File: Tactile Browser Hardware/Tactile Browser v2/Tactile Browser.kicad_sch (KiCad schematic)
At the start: 79 parts, among them SW1 SW_Push, SW10 SW_Push, SW11 SW_Push, SW12 SW_Push, SW13 SW_Push, SW14 SW_Push, SW15 SW_Push, SW16 SW_Push, SW17 SW_Push, SW18 SW_Push, SW19 SW_Push, SW2 SW_Push, SW20 SW_Push, SW3 SW_Push, SW4 SW_Push, SW5 SW_Push, SW6 SW_Push, SW7 SW_Push, SW8 SW_Push, SW9 SW_Push

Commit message: updated module schematic
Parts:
- removed D16, D17: 1N4148, Diode_THT:D_DO-35_SOD27_P7.62mm_Horizontal, symbol Diode:1N4148
- removed Driver10: TB6612FNG, TB6612FNG_THT:TB6612FNG_DualPinHeader_1x8x2_P2.54mm_Row15.24mm_THT, symbol Driver_Motor:TB6612FNG
- removed SW19, SW20: SW_Push, TerminalBlock:TerminalBlock_Xinya_XY308-2.54-2P_1x02_P2.54mm_Horizontal, symbol Switch:SW_Push
- removed Solenoid19, Solenoid20: Conn_01x02_Pin, Connector_JST:JST_VH_B2P-VH-B_1x02_P3.96mm_Vertical, symbol Connector:Conn_01x02_Pin
- added SPI1: Conn_01x03_Pin, TerminalBlock:TerminalBlock_Xinya_XY308-2.54-3P_1x03_P2.54mm_Horizontal, symbol Connector:Conn_01x03_Pin
- renumbered SW9 to SW10, SW10 to SW11, SW17 to SW12, SW11 to SW13, SW12 to SW14, SW13 to SW15, SW14 to SW16, SW15 to SW17, SW16 to SW6, SW6 to SW7, SW7 to SW8, SW8 to SW9
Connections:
- net CLOCK: now also SPI1.1 (Pin_1); no longer A1.16 (D13)
- net Col1: now also A1.2 (D0/RX), D1.1 (K), D19.1 (K), D2.1 (K), D3.1 (K), D4.1 (K), D5.1 (K); no longer A1.7 (D4), SW1.2, SW13.2, SW6.2, SW7.2
- net Col2: now also A1.1 (D1/TX), D14.1 (K), D20.1 (K), D6.1 (K), D7.1 (K), D8.1 (K), D9.1 (K); no longer A1.8 (D5), SW12.2, SW14.2, SW2.2, SW8.2
- net Col3: now also A1.5 (D2), D10.1 (K), D11.1 (K), D12.1 (K), D13.1 (K), D15.1 (K), D18.1 (K); no longer A1.9 (D6), SW15.2, SW18.2, SW3.2, SW9.2
- net DATA: now also SPI1.2 (Pin_2); no longer A1.14 (D11)
- net LATCH: now also SPI1.3 (Pin_3); no longer A1.13 (D10)
- net Row1: now also A1.6 (D3), SW1.2, SW13.2, SW7.2; no longer A1.2 (D0/RX), D1.1 (K), D2.1 (K), D3.1 (K), D4.1 (K), D5.1 (K)
- net Row2: now also A1.7 (D4), SW14.2, SW2.2, SW8.2; no longer A1.1 (D1/TX), D20.1 (K), D6.1 (K), D7.1 (K), D8.1 (K), D9.1 (K)
- net Row3: now also A1.8 (D5), SW15.2, SW3.2, SW9.2; no longer A1.5 (D2), D10.1 (K), D11.1 (K), D12.1 (K), D13.1 (K), D18.1 (K)
- net Row4: now also A1.9 (D6), SW10.2, SW16.2, SW4.2; no longer A1.6 (D3), D14.1 (K), D15.1 (K), D19.1 (K)
- removed net Col4: A1.10 (D7), SW10.2, SW16.2, SW4.2
- net Col5 renamed Row5
- net Row5: now also A1.10 (D7); no longer A1.11 (D8)
- net S19_in1: no longer names the net of IO_5.4 (QE)
- net S19_in2: no longer names the net of IO_5.5 (QF)
- net S20_in1: no longer names the net of IO_5.6 (QG)
- net S20_in2: no longer names the net of IO_5.7 (QH)
- new net Row6: A1.11 (D8), SW12.2, SW18.2, SW6.2
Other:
- moved on the sheet: D1, D10, D11, D12, D13, D14, D15, D18, D19, D2, D20, D3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

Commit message: updated solenoid/keyswitch connectors
for ease of manufacturing
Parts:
- removed SPI1: Conn_01x03_Pin, TerminalBlock:TerminalBlock_Xinya_XY308-2.54-3P_1x03_P2.54mm_Horizontal, symbol Connector:Conn_01x03_Pin
- D1, D2, D3, D4, D5: footprint Diode_THT:D_DO-35_SOD27_P7.62mm_Horizontal -> Diode_SMD:D_SOD-123
- D10: renamed from D9; footprint Diode_THT:D_DO-35_SOD27_P7.62mm_Horizontal -> Diode_SMD:D_SOD-123
- D11: renamed from D20; footprint Diode_THT:D_DO-35_SOD27_P7.62mm_Horizontal -> Diode_SMD:D_SOD-123
- D12: renamed from D14; footprint Diode_THT:D_DO-35_SOD27_P7.62mm_Horizontal -> Diode_SMD:D_SOD-123
- D13: renamed from D18; footprint Diode_THT:D_DO-35_SOD27_P7.62mm_Horizontal -> Diode_SMD:D_SOD-123
- D14: renamed from D10; footprint Diode_THT:D_DO-35_SOD27_P7.62mm_Horizontal -> Diode_SMD:D_SOD-123
- D15: renamed from D11; footprint Diode_THT:D_DO-35_SOD27_P7.62mm_Horizontal -> Diode_SMD:D_SOD-123
- D16: renamed from D12; footprint Diode_THT:D_DO-35_SOD27_P7.62mm_Horizontal -> Diode_SMD:D_SOD-123
- D17: renamed from D13; footprint Diode_THT:D_DO-35_SOD27_P7.62mm_Horizontal -> Diode_SMD:D_SOD-123
- D18: renamed from D15; footprint Diode_THT:D_DO-35_SOD27_P7.62mm_Horizontal -> Diode_SMD:D_SOD-123
- D6: renamed from D19; footprint Diode_THT:D_DO-35_SOD27_P7.62mm_Horizontal -> Diode_SMD:D_SOD-123
- D7: renamed from D6; footprint Diode_THT:D_DO-35_SOD27_P7.62mm_Horizontal -> Diode_SMD:D_SOD-123
- D8: renamed from D7; footprint Diode_THT:D_DO-35_SOD27_P7.62mm_Horizontal -> Diode_SMD:D_SOD-123
- D9: renamed from D8; footprint Diode_THT:D_DO-35_SOD27_P7.62mm_Horizontal -> Diode_SMD:D_SOD-123
- SW1, SW10, SW11, SW12, SW13, SW14, SW15, SW16, SW17, SW18, SW2, SW3, SW4, SW5, SW6, SW7, SW8, SW9: footprint TerminalBlock:TerminalBlock_Xinya_XY308-2.54-2P_1x02_P2.54mm_Horizontal -> Connector_JST:JST_PH_B2B-PH-SM4-TB_1x02-1MP_P2.00mm_Vertical
- Solenoid1: footprint Connector_JST:JST_VH_B2P-VH_1x02_P3.96mm_Vertical -> TerminalBlock_Phoenix:TerminalBlock_Phoenix_MKDS-1,5-2-5.08_1x02_P5.08mm_Horizontal
- Solenoid10, Solenoid11, Solenoid12, Solenoid13, Solenoid14, Solenoid15, Solenoid16, Solenoid17, Solenoid18, Solenoid2, Solenoid3, Solenoid4, Solenoid5, Solenoid6, Solenoid7, Solenoid8, Solenoid9: footprint Connector_JST:JST_VH_B2P-VH-B_1x02_P3.96mm_Vertical -> TerminalBlock_Phoenix:TerminalBlock_Phoenix_MKDS-1,5-2-5.08_1x02_P5.08mm_Horizontal
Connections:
- net 5V: now also IO_2.10 (~{SRCLR}), IO_3.10 (~{SRCLR}), IO_4.10 (~{SRCLR}), IO_5.10 (~{SRCLR})
- net CLOCK: now also A1.16 (D13)
- net DATA: now also A1.14 (D11)
- net LATCH: now also A1.13 (D10)

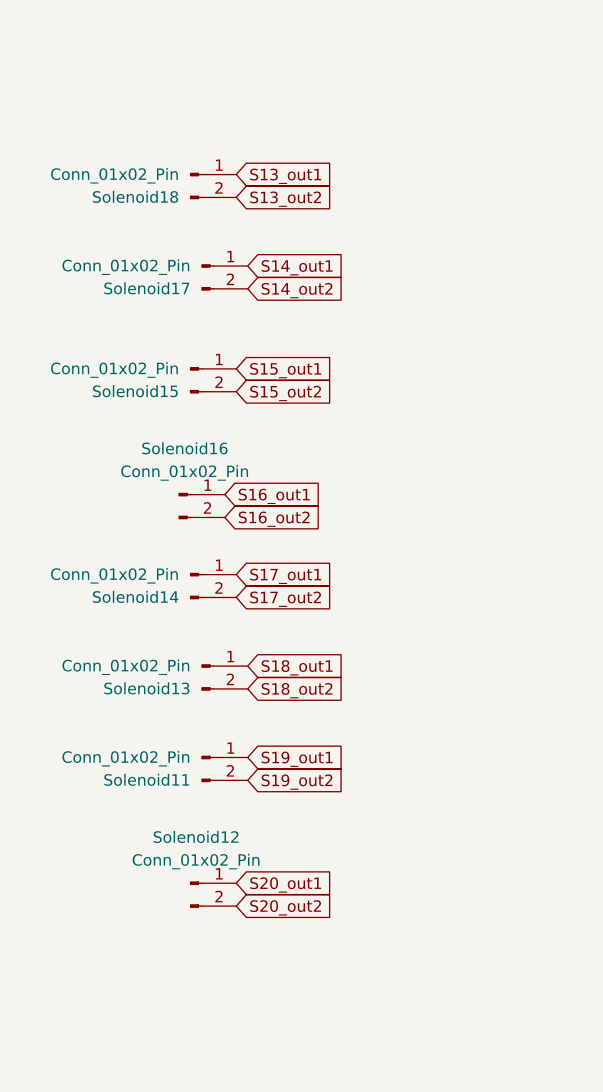
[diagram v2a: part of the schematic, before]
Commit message: Fixed huge solenoid netting issue
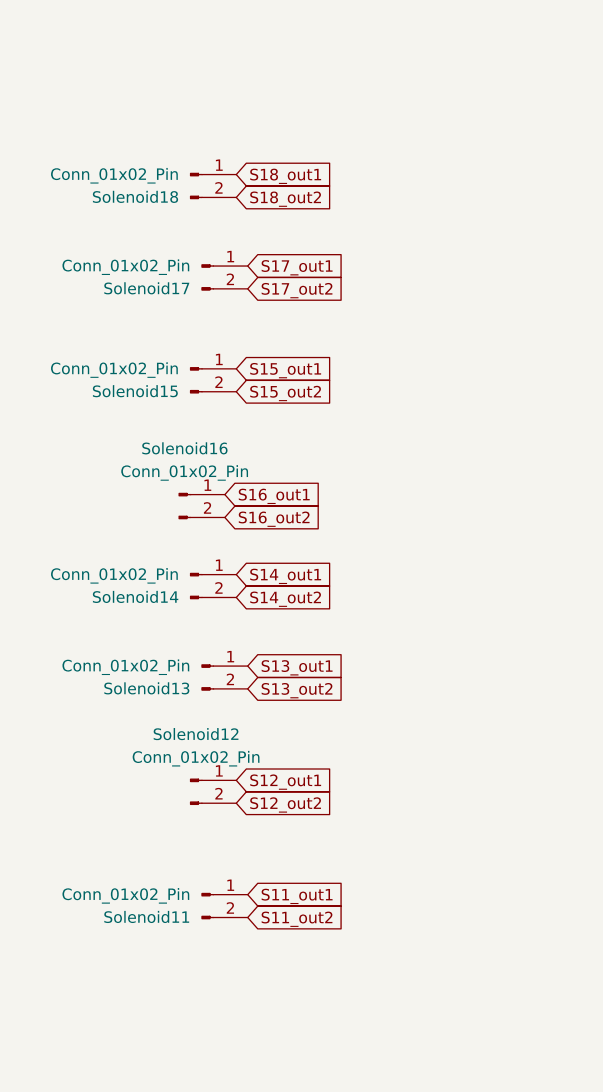
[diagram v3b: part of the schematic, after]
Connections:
- net S19_out1 is gone; now on net S11_out1: Solenoid11.1 (Pin_1)
- net S19_out2 is gone; now on net S11_out2: Solenoid11.2 (Pin_2)
- net S20_out1 is gone; now on net S12_out1: Solenoid12.1 (Pin_1)
- net S20_out2 is gone; now on net S12_out2: Solenoid12.2 (Pin_2)
- net S13_out1: now also Solenoid13.1 (Pin_1); no longer Solenoid18.1 (Pin_1)
- net S13_out2: now also Solenoid13.2 (Pin_2); no longer Solenoid18.2 (Pin_2)
- net S14_out1: now also Solenoid14.1 (Pin_1); no longer Solenoid17.1 (Pin_1)
- net S14_out2: now also Solenoid14.2 (Pin_2); no longer Solenoid17.2 (Pin_2)
- net S17_out1: now also Solenoid17.1 (Pin_1); no longer Solenoid14.1 (Pin_1)
- net S17_out2: now also Solenoid17.2 (Pin_2); no longer Solenoid14.2 (Pin_2)
- net S18_out1: now also Solenoid18.1 (Pin_1); no longer Solenoid13.1 (Pin_1)
- net S18_out2: now also Solenoid18.2 (Pin_2); no longer Solenoid13.2 (Pin_2)
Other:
- moved on the sheet: Solenoid11, Solenoid12
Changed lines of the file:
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@@
 	(global_label "S13_out2"
 		(shape input)
-		(at 58.42 251.46 0)
+		(at 59.69 306.07 0)
 		(fields_autoplaced yes)
 		(effects
@@
 		)
 		(property "Intersheetrefs" "${INTERSHEET_REFS}"
-			(at 70.2345 251.46 0)
+			(at 71.5045 306.07 0)
 			(effects
 				(font
@@
 		)
 	)
-	(global_label "S20_out2"
+	(global_label "S12_out2"
 		(shape input)
-		(at 58.42 330.2 0)
+		(at 58.42 318.77 0)
 		(fields_autoplaced yes)
 		(effects
@@
 		)
 		(property "Intersheetrefs" "${INTERSHEET_REFS}"
-			(at 70.2345 330.2 0)
+			(at 70.2345 318.77 0)
 			(effects
 				(font
@@
 	(global_label "S17_out1"
 		(shape input)
-		(at 58.42 293.37 0)
+		(at 59.69 259.08 0)
 		(fields_autoplaced yes)
 		(effects
@@
 		)
 		(property "Intersheetrefs" "${INTERSHEET_REFS}"
-			(at 70.2345 293.37 0)
+			(at 71.5045 259.08 0)
 			(effects
 				(font
@@
 	(global_label "S14_out2"
 		(shape input)
-		(at 59.69 261.62 0)
+		(at 58.42 295.91 0)
 		(fields_autoplaced yes)
 		(effects
@@
 		)
 		(property "Intersheetrefs" "${INTERSHEET_REFS}"
-			(at 71.5045 261.62 0)
+			(at 70.2345 295.91 0)
 			(effects
 				(font
@@
 	(global_label "S17_out2"
 		(shape input)
-		(at 58.42 295.91 0)
+		(at 59.69 261.62 0)
 		(fields_autoplaced yes)
 		(effects
@@
 		)
 		(property "Intersheetrefs" "${INTERSHEET_REFS}"
-			(at 70.2345 295.91 0)
+			(at 71.5045 261.62 0)
 			(effects
 				(font
@@
 	(global_label "S18_out1"
 		(shape input)
-		(at 59.69 303.53 0)
+		(at 58.42 248.92 0)
 		(fields_autoplaced yes)
 		(effects
@@
 		)
 		(property "Intersheetrefs" "${INTERSHEET_REFS}"
-			(at 71.5045 303.53 0)
+			(at 70.2345 248.92 0)
 			(effects
 				(font
@@
 	(global_label "S14_out1"
 		(shape input)
-		(at 59.69 259.08 0)
+		(at 58.42 293.37 0)
 		(fields_autoplaced yes)
 		(effects
@@
 		)
 		(property "Intersheetrefs" "${INTERSHEET_REFS}"
-			(at 71.5045 259.08 0)
+			(at 70.2345 293.37 0)
 			(effects
 				(font
@@
 		)
 	)
-	(global_label "S19_out2"
+	(global_label "S11_out2"
 		(shape input)
-		(at 59.69 316.23 0)
+		(at 59.69 331.47 0)
 		(fields_autoplaced yes)
 		(effects
@@
 		)
 		(property "Intersheetrefs" "${INTERSHEET_REFS}"
-			(at 71.5045 316.23 0)
+			(at 71.5045 331.47 0)
 			(effects
 				(font
@@
 	(global_label "S18_out2"
 		(shape input)
-		(at 59.69 306.07 0)
+		(at 58.42 251.46 0)
 		(fields_autoplaced yes)
 		(effects
@@
 		)
 		(property "Intersheetrefs" "${INTERSHEET_REFS}"
-			(at 71.5045 306.07 0)
+			(at 70.2345 251.46 0)
 			(effects
 				(font
@@
 		)
 	)
-	(global_label "S19_out1"
+	(global_label "S11_out1"
 		(shape input)
-		(at 59.69 313.69 0)
+		(at 59.69 328.93 0)
 		(fields_autoplaced yes)
 		(effects
@@
 		)
 		(property "Intersheetrefs" "${INTERSHEET_REFS}"
-			(at 71.5045 313.69 0)
+			(at 71.5045 328.93 0)
 			(effects
 				(font
@@
 	(global_label "S13_out1"
 		(shape input)
-		(at 58.42 248.92 0)
+		(at 59.69 303.53 0)
 		(fields_autoplaced yes)
 		(effects
@@
 		)
 		(property "Intersheetrefs" "${INTERSHEET_REFS}"
-			(at 70.2345 248.92 0)
+			(at 71.5045 303.53 0)
 			(effects
 				(font
@@
 		)
 	)
-	(global_label "S20_out1"
+	(global_label "S12_out1"
 		(shape input)
-		(at 58.42 327.66 0)
+		(at 58.42 316.23 0)
 		(fields_autoplaced yes)
 		(effects
@@
 		)
 		(property "Intersheetrefs" "${INTERSHEET_REFS}"
-			(at 70.2345 327.66 0)
+			(at 70.2345 316.23 0)
 			(effects
 				(font
@@
 	(symbol
 		(lib_id "Connector:Conn_01x02_Pin")
-		(at 53.34 327.66 0)
+		(at 53.34 316.23 0)
 		(unit 1)
 		(exclude_from_sim no)
@@
 		(dnp no)
 		(property "Reference" "Solenoid12"
-			(at 53.975 322.58 0)
+			(at 53.975 311.15 0)
 			(effects
 				(font
@@
 		)
 		(property "Value" "Conn_01x02_Pin"
-			(at 53.975 325.12 0)
+			(at 53.975 313.69 0)
 			(effects
 				(font
@@
 		)
 		(property "Footprint" "TerminalBlock_Phoenix:TerminalBlock_Phoenix_MKDS-1,5-2-5.08_1x02_P5.08mm_Horizontal"
-			(at 53.34 327.66 0)
+			(at 53.34 316.23 0)
 			(effects
 				(font
@@
 		)
 		(property "Datasheet" "~"
-			(at 53.34 327.66 0)
+			(at 53.34 316.23 0)
 			(effects
 				(font
@@
 		)
 		(property "Description" "Generic connector, single row, 01x02, script generated"
-			(at 53.34 327.66 0)
+			(at 53.34 316.23 0)
 			(effects
 				(font
@@
 	(symbol
 		(lib_id "Connector:Conn_01x02_Pin")
-		(at 54.61 313.69 0)
+		(at 54.61 328.93 0)
 		(unit 1)
 		(exclude_from_sim no)
@@
 		(fields_autoplaced yes)
 		(property "Reference" "Solenoid11"
-			(at 53.34 316.2301 0)
+			(at 53.34 331.4701 0)
 			(effects
 				(font
@@
 		)
 		(property "Value" "Conn_01x02_Pin"
-			(at 53.34 313.6901 0)
+			(at 53.34 328.9301 0)
 			(effects
 				(font
@@
 		)
 		(property "Footprint" "TerminalBlock_Phoenix:TerminalBlock_Phoenix_MKDS-1,5-2-5.08_1x02_P5.08mm_Horizontal"
-			(at 54.61 313.69 0)
+			(at 54.61 328.93 0)
 			(effects
 				(font
@@
 		)
 		(property "Datasheet" "~"
-			(at 54.61 313.69 0)
+			(at 54.61 328.93 0)
 			(effects
 				(font
@@
 		)
 		(property "Description" "Generic connector, single row, 01x02, script generated"
-			(at 54.61 313.69 0)
+			(at 54.61 328.93 0)
 			(effects
 				(font

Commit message: a ton of work on the pcb
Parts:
- IO_1, IO_2, IO_3, IO_4, IO_5: footprint Package_DIP:DIP-16_W7.62mm -> Package_SO:JEITA_SOIC-16_3.9x9.9mm_P1.27mm
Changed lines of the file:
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@@
 			)
 		)
-		(property "Footprint" "Package_DIP:DIP-16_W7.62mm"
+		(property "Footprint" "Package_SO:JEITA_SOIC-16_3.9x9.9mm_P1.27mm"
 			(at 238.76 154.94 0)
 			(effects
@@
 			)
 		)
-		(property "Footprint" "Package_DIP:DIP-16_W7.62mm"
+		(property "Footprint" "Package_SO:JEITA_SOIC-16_3.9x9.9mm_P1.27mm"
 			(at 283.21 300.99 0)
 			(effects
@@
 			)
 		)
-		(property "Footprint" "Package_DIP:DIP-16_W7.62mm"
+		(property "Footprint" "Package_SO:JEITA_SOIC-16_3.9x9.9mm_P1.27mm"
 			(at 262.89 346.71 0)
 			(effects
@@
 			)
 		)
-		(property "Footprint" "Package_DIP:DIP-16_W7.62mm"
+		(property "Footprint" "Package_SO:JEITA_SOIC-16_3.9x9.9mm_P1.27mm"
 			(at 236.22 300.99 0)
 			(effects
@@
 			)
 		)
-		(property "Footprint" "Package_DIP:DIP-16_W7.62mm"
+		(property "Footprint" "Package_SO:JEITA_SOIC-16_3.9x9.9mm_P1.27mm"
 			(at 285.75 156.21 0)
 			(effects

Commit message: integrated drivers
added schottky diodes, bulk & decoupling capacitors
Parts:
- added 100nF1, 100nF10, 100nF11, 100nF12, 100nF13, 100nF14, 100nF15, 100nF2, 100nF3, 100nF4, 100nF5, 100nF6, 100nF7, 100nF8, 100nF9, C2_100nF1, C2_100nF2, C2_100nF3: C, Capacitor_SMD:C_0805_2012Metric, symbol Device:C
- added 470uF_25V1, 470uF_25V2, 470uF_25V3, 470uF_25V4, 470uF_25V5, 470uF_25V6, 470uF_25V7, 470uF_25V8, 470uF_25V9: C_Polarized, Capacitor_SMD:CP_Elec_8x10, symbol Device:C_Polarized
- added DS1, DS10, DS11, DS12, DS13, DS14, DS15, DS16, DS17, DS18, DS19, DS2, DS20, DS21, DS22, DS23, DS24, DS25, DS26, DS27, DS28, DS29, DS3, DS30, DS31, DS32, DS33, DS34, DS35, DS36, DS4, DS5, DS6, DS7, DS8, DS9: D_Schottky, Diode_SMD:D_SMA, symbol Device:D_Schottky
- Driver1, Driver2, Driver3, Driver4, Driver5, Driver6, Driver7, Driver8, Driver9: footprint TB6612FNG_THT:TB6612FNG_DualPinHeader_1x8x2_P2.54mm_Row15.24mm_THT -> Package_SO:SSOP-24_5.3x8.2mm_P0.65mm
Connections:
- net 12V: now also 100nF1.1, 100nF10.1, 100nF12.1, 100nF14.1, 100nF2.1, 100nF3.1, 100nF4.1, 100nF6.1, 100nF8.1, 470uF_25V1.1, 470uF_25V2.1, 470uF_25V3.1, 470uF_25V4.1, 470uF_25V5.1, 470uF_25V6.1, 470uF_25V7.1, 470uF_25V8.1, 470uF_25V9.1, DS1.1 (K), DS10.1 (K), DS11.1 (K), DS12.1 (K), DS13.1 (K), DS14.1 (K), DS15.1 (K), DS16.1 (K), DS17.1 (K), DS18.1 (K), DS19.1 (K), DS2.1 (K), DS20.1 (K), DS21.1 (K), DS22.1 (K), DS23.1 (K), DS24.1 (K), DS25.1 (K), DS26.1 (K), DS27.1 (K), DS28.1 (K), DS29.1 (K), DS3.1 (K), DS30.1 (K), DS31.1 (K), DS32.1 (K), DS33.1 (K), DS34.1 (K), DS35.1 (K), DS36.1 (K), DS4.1 (K), DS5.1 (K), DS6.1 (K), DS7.1 (K), DS8.1 (K), DS9.1 (K)
- net 5V: now also 100nF11.1, 100nF13.1, 100nF15.1, 100nF5.1, 100nF7.1, 100nF9.1, C2_100nF1.2, C2_100nF2.2, C2_100nF3.2
- net GND: now also 100nF1.2, 100nF10.2, 100nF11.2, 100nF12.2, 100nF13.2, 100nF14.2, 100nF15.2, 100nF2.2, 100nF3.2, 100nF4.2, 100nF5.2, 100nF6.2, 100nF7.2, 100nF8.2, 100nF9.2, 470uF_25V1.2, 470uF_25V2.2, 470uF_25V3.2, 470uF_25V4.2, 470uF_25V5.2, 470uF_25V6.2, 470uF_25V7.2, 470uF_25V8.2, 470uF_25V9.2, C2_100nF1.1, C2_100nF2.1, C2_100nF3.1
- net S10_out1: now also DS19.2 (A)
- net S10_out2: now also DS20.2 (A)
- net S11_out1: now also DS21.2 (A)
- net S11_out2: now also DS22.2 (A)
- net S12_out1: now also DS23.2 (A)
- net S12_out2: now also DS24.2 (A)
- net S13_out1: now also DS25.2 (A)
- net S13_out2: now also DS26.2 (A)
- net S14_out1: now also DS27.2 (A)
- net S14_out2: now also DS28.2 (A)
- net S15_out1: now also DS29.2 (A)
- net S15_out2: now also DS30.2 (A)
- net S16_out1: now also DS31.2 (A)
- net S16_out2: now also DS32.2 (A)
- net S17_out1: now also DS33.2 (A)
- net S17_out2: now also DS34.2 (A)
- net S18_out1: now also DS35.2 (A)
- net S18_out2: now also DS36.2 (A)
- net S1_out1: now also DS1.2 (A)
- net S1_out2: now also DS2.2 (A)
- net S2_out1: now also DS3.2 (A)
- net S2_out2: now also DS4.2 (A)
- net S3_out1: now also DS5.2 (A)
- net S3_out2: now also DS6.2 (A)
- net S4_out1: now also DS7.2 (A)
- net S4_out2: now also DS8.2 (A)
- net S5_out1: now also DS12.2 (A)
- net S5_out2: now also DS11.2 (A)
- net S6_out1: now also DS10.2 (A)
- net S6_out2: now also DS9.2 (A)
- net S7_out1: now also DS13.2 (A)
- net S7_out2: now also DS14.2 (A)
- net S8_out1: now also DS15.2 (A)
- net S8_out2: now also DS16.2 (A)
- net S9_out1: now also DS17.2 (A)
- net S9_out2: now also DS18.2 (A)
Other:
- moved on the sheet: 12V_supply1, 5V_logic_rail1, A1, D1, D10, D11, D12, D13, D14, D15, D16, D17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
